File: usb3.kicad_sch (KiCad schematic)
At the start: 45 parts, among them J5 WE_632723300011_alt_symbol, Q4 NX138BKMYL, U17 HD3SS3220, U18 AP22615, U19 TPD4E05U06QDQARQ1, U20 TPD4E05U06QDQARQ1, U21 TPD4E05U06QDQARQ1

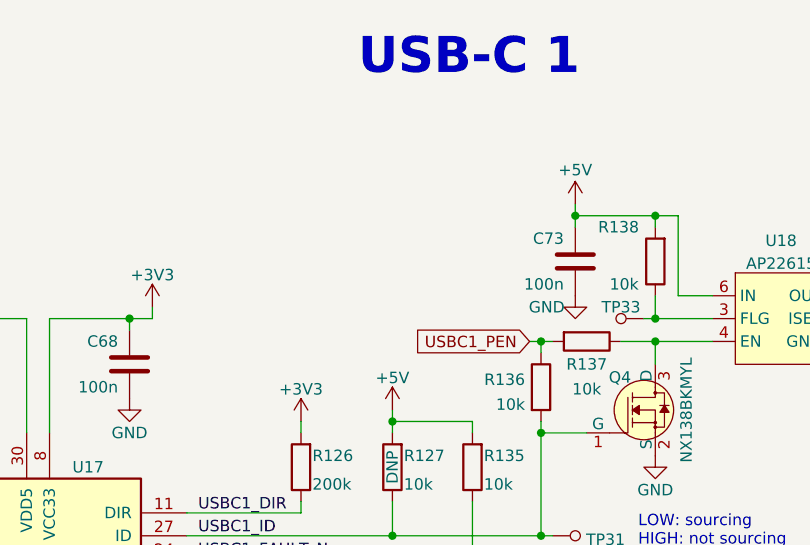
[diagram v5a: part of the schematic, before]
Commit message: Added pull-up resistor to USBC1_PEN [#40393]
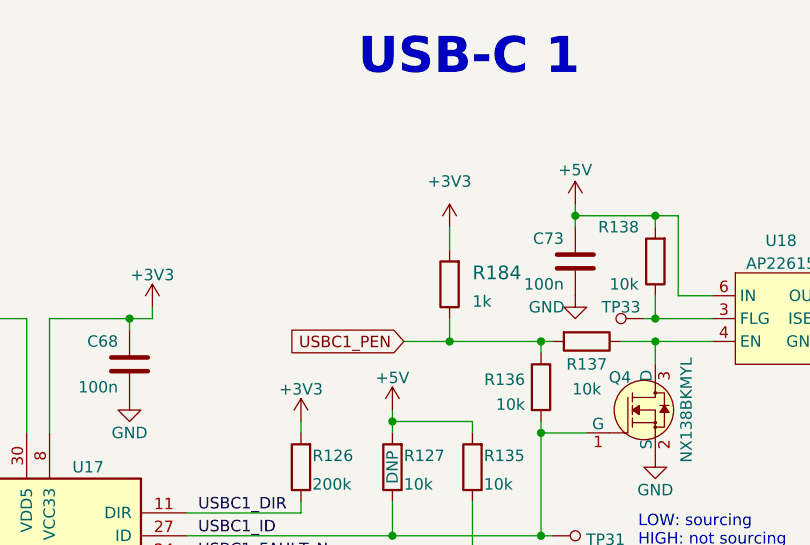
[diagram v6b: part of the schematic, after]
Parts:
- added R184: R_1k_0402, jetson-orin-baseboard-footprints:0402-res, symbol jetson-orin-baseboard:R_1k_0402
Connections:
- net +3V3: now also R184.2
- net USBC1_PEN: now also R184.1
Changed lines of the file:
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@@
   (junction (at 170.18 97.79) (diameter 0) (color 0 0 0 0)
   )
+  (junction (at 205.74 100.33) (diameter 0) (color 0 0 0 0)
+  )
   (junction (at 160.02 190.5) (diameter 0) (color 0 0 0 0)
   )
@@
     (stroke (width 0) (type default) (color 0 0 0 0))
   )
-  (wire (pts (xy 214.63 100.33) (xy 215.9 100.33))
+  (wire (pts (xy 200.66 100.33) (xy 205.74 100.33))
     (stroke (width 0) (type default) (color 0 0 0 0))
   )
@@
     (stroke (width 0) (type default) (color 0 0 0 0))
   )
+  (wire (pts (xy 205.74 97.79) (xy 205.74 100.33))
+    (stroke (width 0) (type default) (color 0 0 0 0))
+  )
   (wire (pts (xy 271.78 162.56) (xy 271.78 185.42))
     (stroke (width 0) (type default) (color 0 0 0 0))
@@
     (stroke (width 0) (type default) (color 0 0 0 0))
   )
+  (wire (pts (xy 205.74 87.63) (xy 205.74 90.17))
+    (stroke (width 0) (type default) (color 0 0 0 0))
+  )
   (wire (pts (xy 274.32 157.48) (xy 289.56 157.48))
     (stroke (width 0) (type default) (color 0 0 0 0))
@@
     (stroke (width 0) (type default) (color 0 0 0 0))
   )
+  (wire (pts (xy 205.74 100.33) (xy 215.9 100.33))
+    (stroke (width 0) (type default) (color 0 0 0 0))
+  )
   (wire (pts (xy 228.6 86.36) (xy 228.6 87.63))
     (stroke (width 0) (type default) (color 0 0 0 0))
@@
     )
   )
-  (global_label "USBC1_PEN" (shape input) (at 214.63 100.33 180)
+  (global_label "USBC1_PEN" (shape input) (at 200.66 100.33 180)
     (effects (font (size 1.27 1.27)) (justify right))
-    (property "Intersheet References" "${INTERSHEET_REFS}" (id 0) (at 200.66 100.33 0)
+    (property "Intersheet References" "${INTERSHEET_REFS}" (id 0) (at 186.69 100.33 0)
       (effects (font (size 1.27 1.27)) (justify right))
     )
@@
     (pin "2")
   )
+  (symbol (lib_id "jetson-orin-baseboard:R_1k_0402") (at 205.74 93.98 90) (unit 1)
+    (in_bom yes) (on_board yes) (fields_autoplaced)
+    (property "Reference" "R184" (id 0) (at 208.28 92.71 90)
+      (effects (font (size 1.524 1.524)) (justify right))
+    )
+    (property "Value" "R_1k_0402" (id 1) (at 209.55 93.98 0)
+      (effects (font (size 1.524 1.524)) hide)
+    )
+    (property "Footprint" "jetson-orin-baseboard-footprints:0402-res" (id 2) (at 200.66 88.9 0)
+      (effects (font (size 1.524 1.524)) (justify left) hide)
+    )
+    (property "Datasheet" "" (id 3) (at 205.74 93.98 0)
+      (effects (font (size 1.27 1.27)) hide)
+    )
+    (property "Manufacturer" "BOURNS" (id 4) (at 195.58 88.9 0)
+      (effects (font (size 1.524 1.524)) (justify left) hide)
+    )
+    (property "MPN" "CR0402-FX-1001GLF" (id 5) (at 198.12 88.9 0)
+      (effects (font (size 1.524 1.524)) (justify left) hide)
+    )
+    (property "Val" "1k" (id 6) (at 208.28 95.8849 90)
+      (effects (font (size 1.27 1.27)) (justify right))
+    )
+    (pin "1")
+    (pin "2")
+  )
   (symbol (lib_id "jetson-orin-baseboard:GND") (at 306.07 118.11 0) (unit 1)
     (in_bom yes) (on_board yes)
@@
     (pin "2")
   )
+  (symbol (lib_id "jetson-orin-baseboard:+3V3") (at 205.74 87.63 0) (unit 1)
+    (in_bom yes) (on_board yes) (fields_autoplaced)
+    (property "Reference" "#PWR0289" (id 0) (at 205.74 91.44 0)
+      (effects (font (size 1.27 1.27)) hide)
+    )
+    (property "Value" "+3V3" (id 1) (at 205.74 82.55 0))
+    (property "Footprint" "" (id 2) (at 205.74 87.63 0)
+      (effects (font (size 1.27 1.27)) hide)
+    )
+    (property "Datasheet" "" (id 3) (at 205.74 87.63 0)
+      (effects (font (size 1.27 1.27)) hide)
+    )
+    (pin "1")
+  )
   (symbol (lib_id "jetson-orin-baseboard:TP_SMD_0_75MM") (at 224.79 97.79 270) (unit 1)

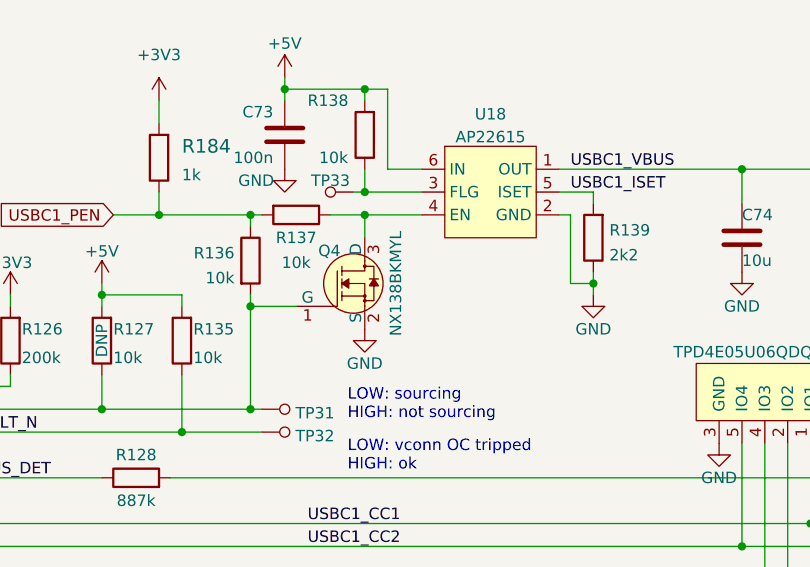
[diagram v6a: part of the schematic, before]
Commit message: Replaced NX138BKMYL with PJE138K transistor [#40527]
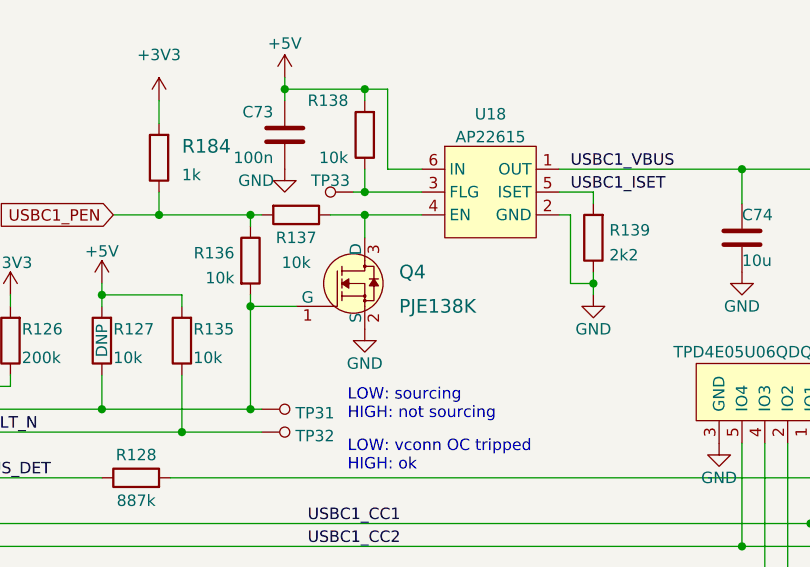
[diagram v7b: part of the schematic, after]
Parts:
- removed Q4: NX138BKMYL, jetson-orin-baseboard-footprints:DFN1006-3, symbol jetson-orin-baseboard:NX138BKMYL
- added Q4: PJE138K, antmicro-footprints:SOT-523, symbol antmicroTransistorsFETsMOSFETsSingle:PJE138K
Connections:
- net GND: now also Q4.2 (S)
- net USBC1_ID: now also Q4.1 (G)
- net at R137.1, U18.4 (EN): now also Q4.3 (D)
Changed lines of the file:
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@@
     (pin "1")
+  )
+  (symbol (lib_id "antmicroTransistorsFETsMOSFETsSingle:PJE138K") (at 228.6 107.95 0) (unit 1)
+    (in_bom yes) (on_board yes) (fields_autoplaced)
+    (property "Reference" "Q4" (id 0) (at 232.41 106.68 0)
+      (effects (font (size 1.524 1.524)) (justify left))
+    )
+    (property "Value" "PJE138K" (id 1) (at 232.41 110.49 0)
+      (effects (font (size 1.524 1.524)) (justify left))
+    )
+    (property "Footprint" "antmicro-footprints:SOT-523" (id 2) (at 233.68 102.87 0)
+      (effects (font (size 1.524 1.524)) (justify left) hide)
+    )
+    (property "Datasheet" "https://www.mouser.pl/datasheet/2/1057/PJE138K-1876698.pdf" (id 3) (at 233.68 100.33 0)
+      (effects (font (size 1.524 1.524)) (justify left) hide)
+    )
+    (property "MPN" "PJE138K_R1_00001" (id 4) (at 245.11 97.79 0)
+      (effects (font (size 1.524 1.524)) (justify left) hide)
+    )
+    (property "Manufacturer" "Panjit" (id 5) (at 233.68 97.79 0)
+      (effects (font (size 1.524 1.524)) (justify left) hide)
+    )
+    (pin "1")
+    (pin "2")
+    (pin "3")
   )
   (symbol (lib_id "jetson-orin-baseboard:R_0R_0402") (at 85.09 187.96 90) (unit 1)
@@
     (pin "1")
   )
-  (symbol (lib_id "jetson-orin-baseboard:NX138BKMYL") (at 228.6 107.95 0) (unit 1)
-    (in_bom yes) (on_board yes) (fields_autoplaced)
-    (property "Reference" "Q4" (id 0) (at 225.9076 104.3178 0)
-      (effects (font (size 1.27 1.27)) (justify right))
-    )
-    (property "Value" "NX138BKMYL" (id 1) (at 232.0544 107.95 90))
-    (property "Footprint" "jetson-orin-baseboard-footprints:DFN1006-3" (id 2) (at 233.68 102.87 0)
-      (effects (font (size 1.524 1.524)) (justify left) hide)
-    )
-    (property "Datasheet" "https://www.mouser.pl/datasheet/2/916/NX138BKM-1919503.pdf" (id 3) (at 233.68 100.33 0)
-      (effects (font (size 1.524 1.524)) (justify left) hide)
-    )
-    (property "MPN" "NX138BKMYL" (id 4) (at 233.68 95.25 0)
-      (effects (font (size 1.524 1.524)) (justify left) hide)
-    )
-    (property "Manufacturer" "Nexperia" (id 5) (at 233.68 80.01 0)
-      (effects (font (size 1.524 1.524)) (justify left) hide)
-    )
-    (pin "1")
-    (pin "2")
-    (pin "3")
-  )
   (symbol (lib_id "jetson-orin-baseboard:C_100n_0402") (at 201.93 177.8 90) (unit 1)

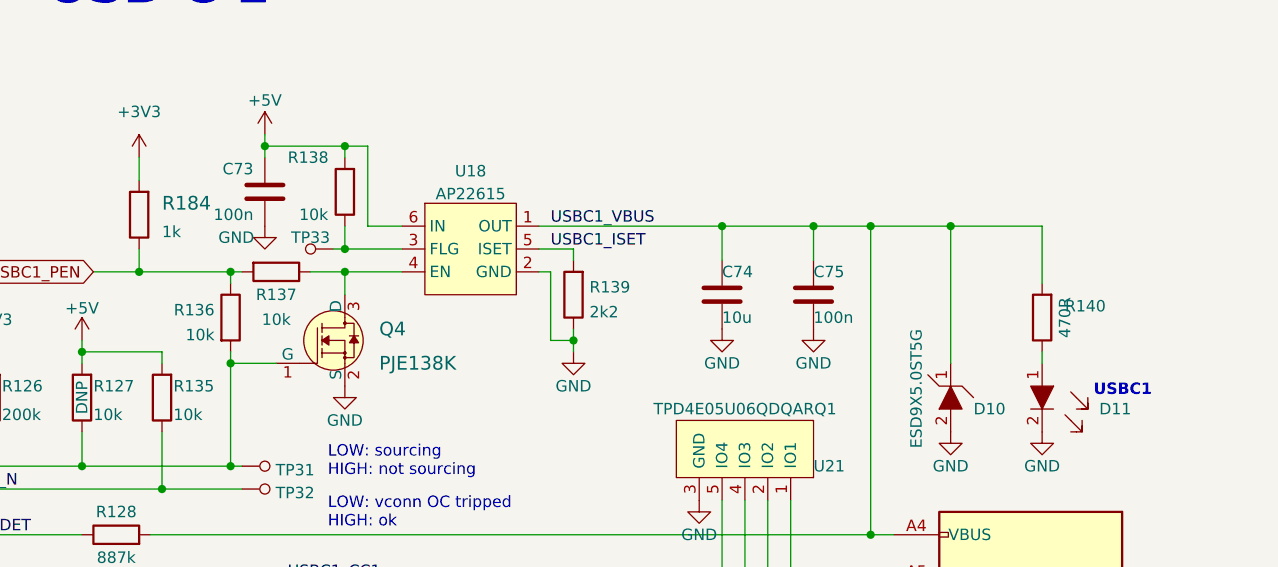
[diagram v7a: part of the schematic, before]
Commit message: BOM reduction [#40581]
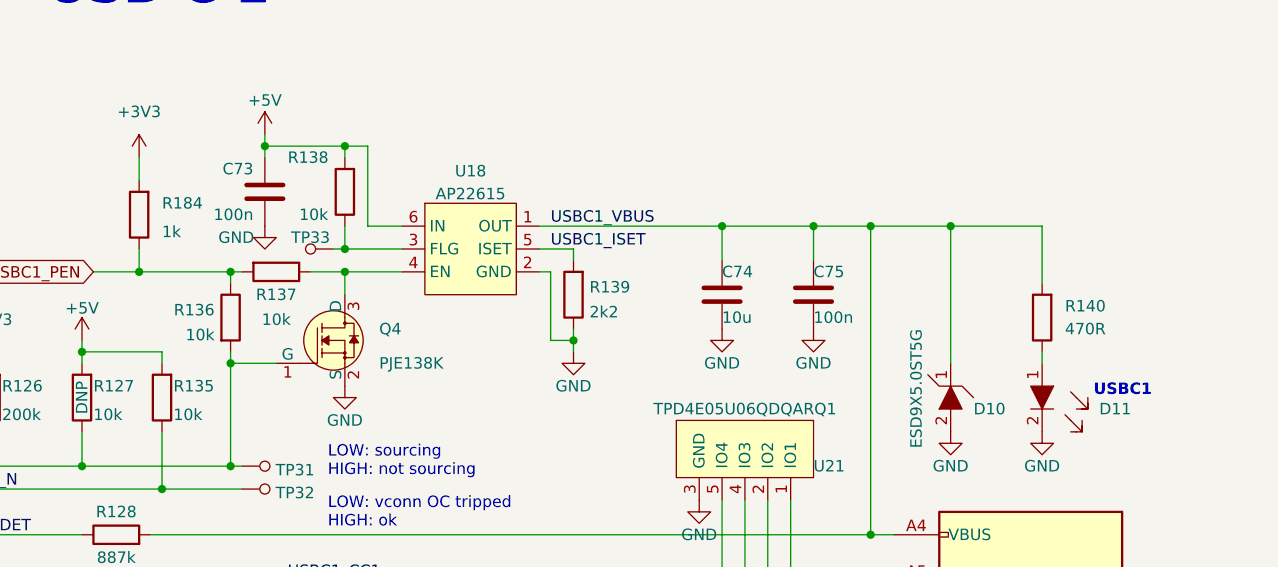
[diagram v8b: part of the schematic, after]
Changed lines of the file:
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@@
   (symbol (lib_id "jetson-orin-baseboard:R_470R_0402") (at 306.07 105.41 90) (unit 1)
     (in_bom yes) (on_board yes) (fields_autoplaced)
-    (property "Reference" "R140" (id 0) (at 308.61 104.14 90)
+    (property "Reference" "R140" (id 0) (at 308.61 104.1399 90)
       (effects (font (size 1.27 1.27)) (justify right))
     )
     (property "Value" "R_470R_0402" (id 1) (at 309.88 105.41 0)
-      (effects (font (size 1.524 1.524)) hide)
+      (effects (font (size 1.27 1.27)) hide)
     )
     (property "Footprint" "jetson-orin-baseboard-footprints:0402-res" (id 2) (at 300.99 100.33 0)
@@
       (effects (font (size 1.524 1.524)) (justify left) hide)
     )
-    (property "Val" "470R" (id 6) (at 308.61 105.41 0))
+    (property "Val" "470R" (id 6) (at 308.61 106.6799 90)
+      (effects (font (size 1.27 1.27)) (justify right))
+    )
     (pin "1")
     (pin "2")
@@
     (in_bom yes) (on_board yes) (fields_autoplaced)
     (property "Reference" "Q4" (id 0) (at 232.41 106.68 0)
-      (effects (font (size 1.524 1.524)) (justify left))
+      (effects (font (size 1.27 1.27)) (justify left))
     )
     (property "Value" "PJE138K" (id 1) (at 232.41 110.49 0)
-      (effects (font (size 1.524 1.524)) (justify left))
+      (effects (font (size 1.27 1.27)) (justify left))
     )
     (property "Footprint" "antmicro-footprints:SOT-523" (id 2) (at 233.68 102.87 0)
@@
     (in_bom yes) (on_board yes) (fields_autoplaced)
     (property "Reference" "R184" (id 0) (at 208.28 92.71 90)
-      (effects (font (size 1.524 1.524)) (justify right))
+      (effects (font (size 1.27 1.27)) (justify right))
     )
     (property "Value" "R_1k_0402" (id 1) (at 209.55 93.98 0)
-      (effects (font (size 1.524 1.524)) hide)
+      (effects (font (size 1.27 1.27)) hide)
     )
     (property "Footprint" "jetson-orin-baseboard-footprints:0402-res" (id 2) (at 200.66 88.9 0)
